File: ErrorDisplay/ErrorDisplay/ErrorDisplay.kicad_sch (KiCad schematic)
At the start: 0 parts

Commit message: Close Placement of Motors. Need Mechanical Fit check first
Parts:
- added H1, H2, H3, H4: MountingHole, MountingHole:MountingHole_4.3mm_M4, symbol Mechanical:MountingHole
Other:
- added sheet Motors (Motors.kicad_sch)
- note added: "Mounting Bracket to the faceplate"

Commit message: WIP - Test build for the Stepper Driver
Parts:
- added J4: Conn_01x04_Pin, Library:CONN_70551-xxxx_04_MOL, symbol Connector:Conn_01x04_Pin
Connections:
- new net CANH: J4.2 (Pin_2)
- new net CANL: J4.3 (Pin_3)
- new net CAN_VCC: J4.1 (Pin_1)
- new net GND: J4.4 (Pin_4)
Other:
- added sheet CANBus (CANBus.kicad_sch)
- added sheet MCU (MCU.kicad_sch)
- added sheet Power (Power.kicad_sch)

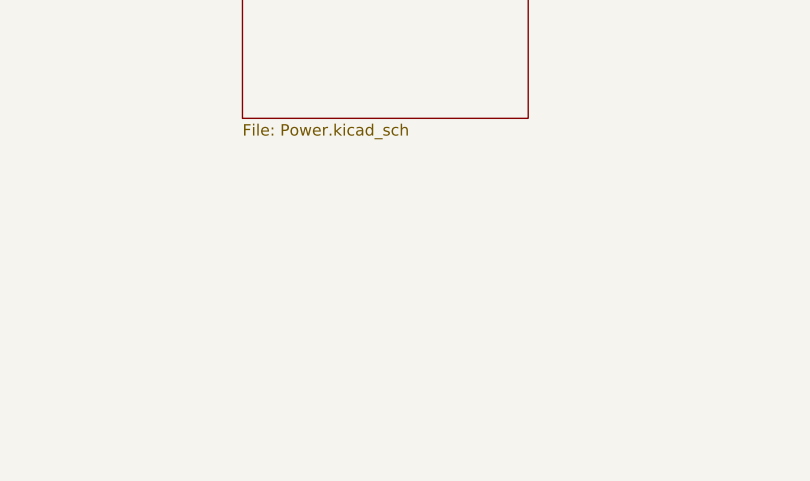
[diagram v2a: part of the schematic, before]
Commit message: LEDs outlined. Colors Chosen.
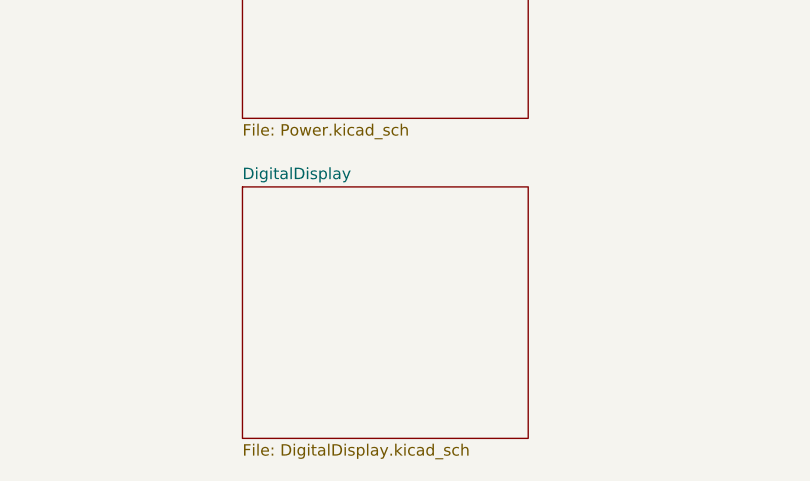
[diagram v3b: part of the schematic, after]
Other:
- added sheet DigitalDisplay (DigitalDisplay.kicad_sch)
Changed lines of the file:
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@@
+		)
+	)
+	(sheet
+		(at 68.58 162.56)
+		(size 31.75 27.94)
+		(fields_autoplaced yes)
+		(stroke
+			(width 0.1524)
+			(type solid)
+		)
+		(fill
+			(color 0 0 0 0.0000)
+		)
+		(property "Sheetname" "DigitalDisplay"
+			(at 68.58 161.8484 0)
+			(effects
+				(font
+					(size 1.27 1.27)
+				)
+				(justify left bottom)
+			)
+		)
+		(property "Sheetfile" "DigitalDisplay.kicad_sch"
+			(at 68.58 191.0846 0)
+			(effects
+				(font
+					(size 1.27 1.27)
+				)
+				(justify left top)
+			)
+		)
+		(instances
+			(project "ErrorDisplay"
+				(path "/96a9355b-dc07-421e-8192-6c91221ac38a"
+					(page "6")
+				)
+			)
 		)
 	)

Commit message: WIP checkin
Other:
- sheet DigitalDisplay ports: added SCL, SDA; removed none
- sheet MCU ports: added SCL, SDA; removed none
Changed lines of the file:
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@@
+		)
+	)
+	(label "SDA"
+		(at 100.33 166.37 0)
+		(fields_autoplaced yes)
+		(effects
+			(font
+				(size 1.27 1.27)
+			)
+			(justify left bottom)
 		)
 	)
@@
 			)
 			(justify left bottom)
+		)
+	)
+	(label "SCL"
+		(at 134.62 151.13 180)
+		(fields_autoplaced yes)
+		(effects
+			(font
+				(size 1.27 1.27)
+			)
+			(justify right bottom)
+		)
+	)
+	(label "SCL"
+		(at 100.33 163.83 0)
+		(fields_autoplaced yes)
+		(effects
+			(font
+				(size 1.27 1.27)
+			)
+			(justify left bottom)
+		)
+	)
+	(label "SDA"
+		(at 134.62 153.67 180)
+		(fields_autoplaced yes)
+		(effects
+			(font
+				(size 1.27 1.27)
+			)
+			(justify right bottom)
 		)
 	)
@@
 		)
 		(property "Sheetfile" "MCU.kicad_sch"
-			(at 132.334 154.94 90)
+			(at 132.334 142.24 90)
 			(effects
 				(font
@@
 				)
 				(justify right)
+			)
+		)
+		(pin "SDA" input
+			(at 134.62 153.67 180)
+			(effects
+				(font
+					(size 1.27 1.27)
+				)
+				(justify left)
+			)
+		)
+		(pin "SCL" input
+			(at 134.62 151.13 180)
+			(effects
+				(font
+					(size 1.27 1.27)
+				)
+				(justify left)
 			)
 		)
@@
 			)
 		)
+		(pin "SCL" input
+			(at 100.33 163.83 0)
+			(effects
+				(font
+					(size 1.27 1.27)
+				)
+				(justify right)
+			)
+		)
+		(pin "SDA" input
+			(at 100.33 166.37 0)
+			(effects
+				(font
+					(size 1.27 1.27)
+				)
+				(justify right)
+			)
+		)

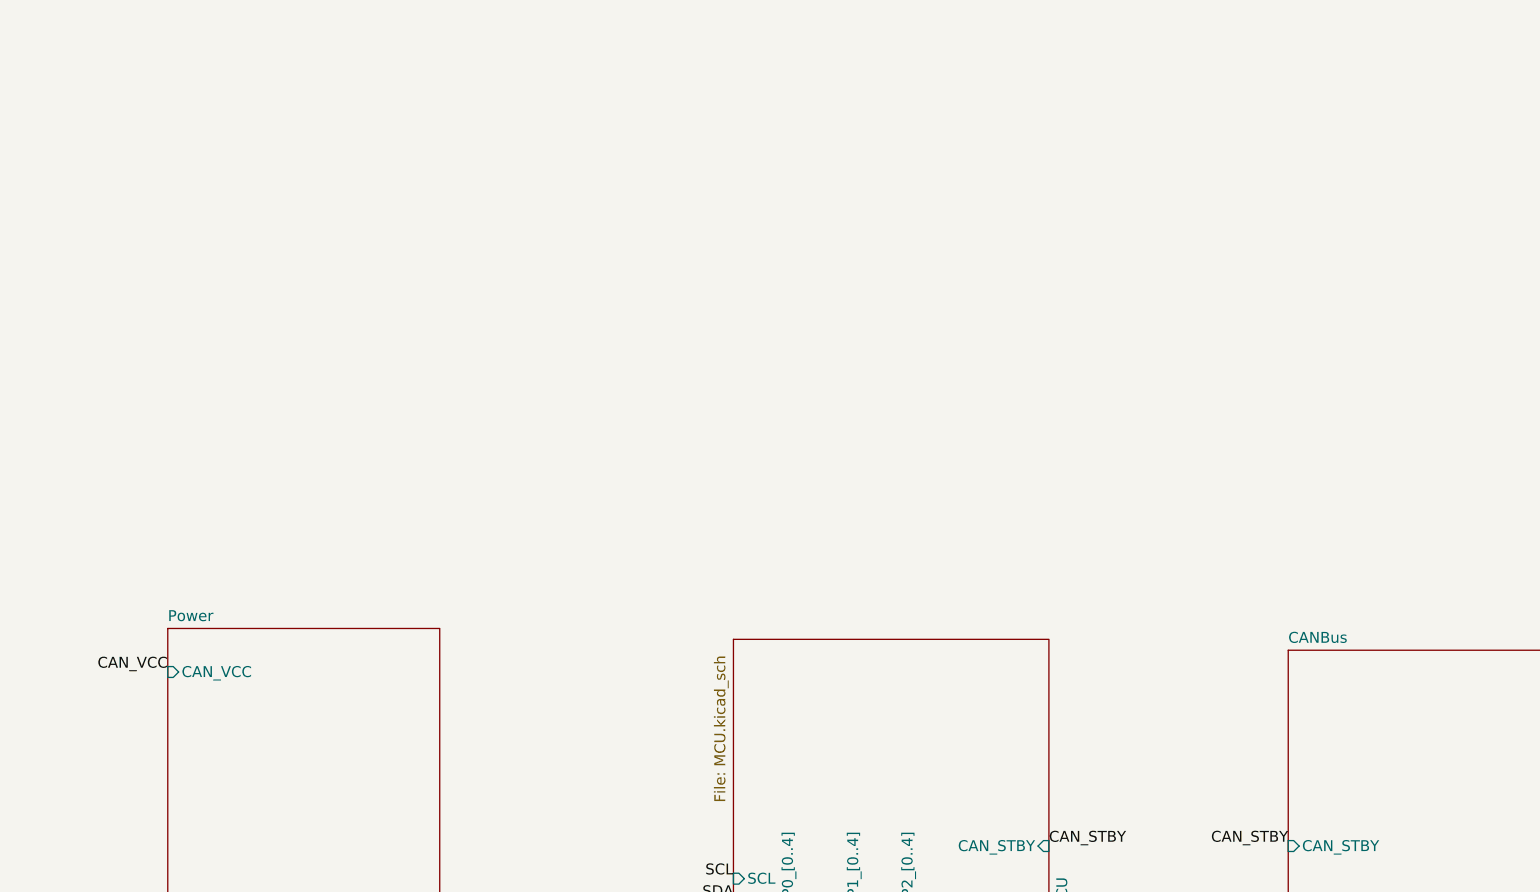
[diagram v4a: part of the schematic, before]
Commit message: Added Buzzer, Fet Footprint, and pulled backlighting
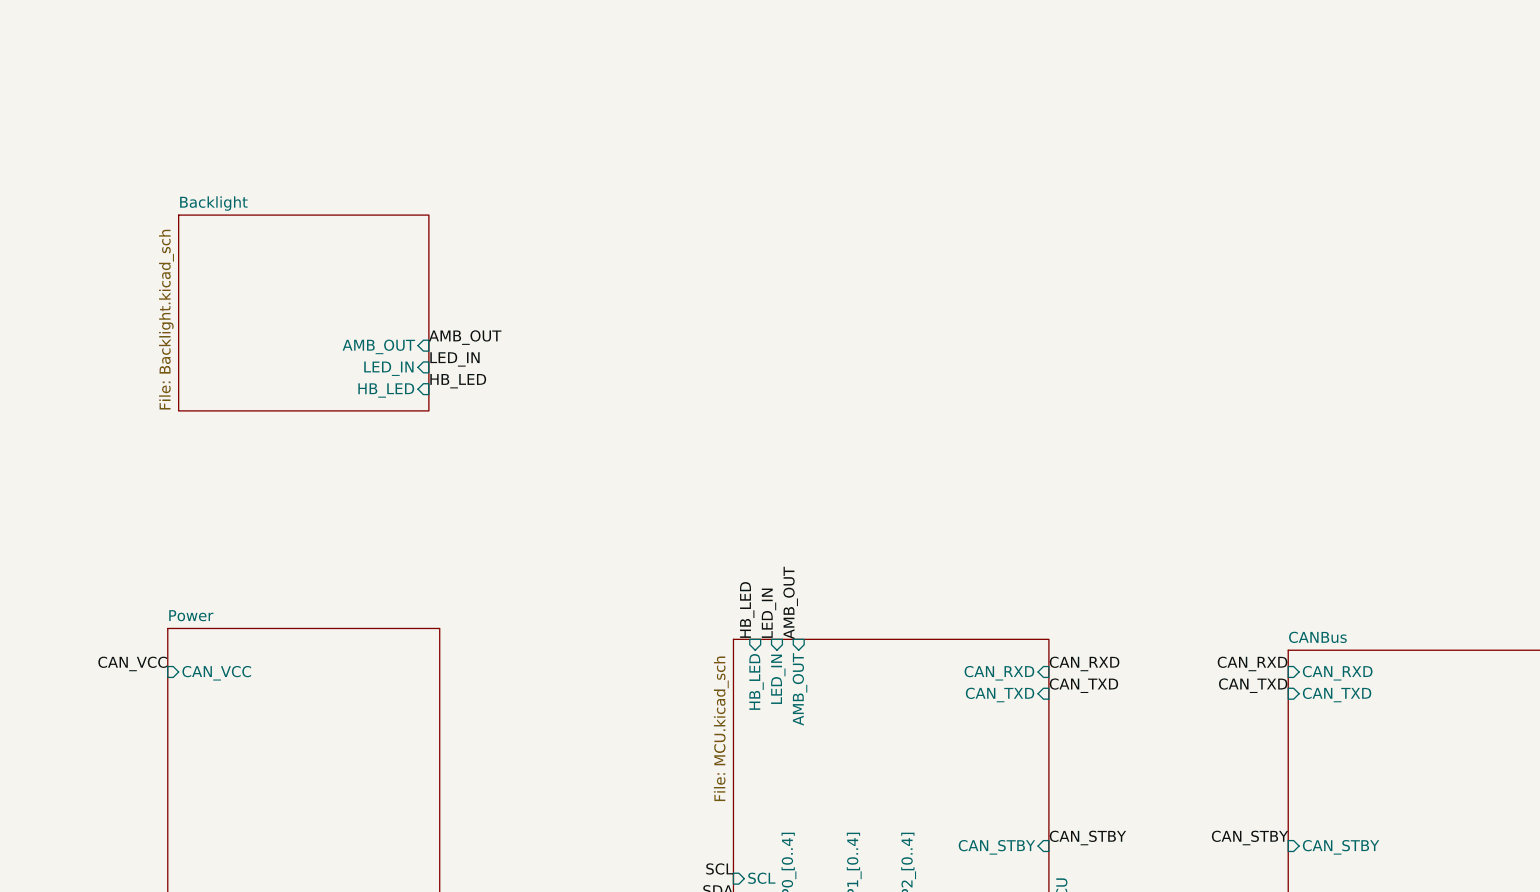
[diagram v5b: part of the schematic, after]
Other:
- added sheet Backlight (Backlight.kicad_sch)
- sheet CANBus ports: added CAN_RXD, CAN_TXD; removed none
- sheet MCU ports: added AMB_OUT, CAN_RXD, CAN_TXD, HB_LED, LED_IN; removed none
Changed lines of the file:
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@@
 	(label "CAN_VCC"
 		(at 271.78 19.05 180)
-		(fields_autoplaced yes)
 		(effects
 			(font
@@
 	(label "CANH"
 		(at 238.76 124.46 90)
-		(fields_autoplaced yes)
 		(effects
 			(font
@@
 	(label "SDA"
 		(at 100.33 166.37 0)
-		(fields_autoplaced yes)
 		(effects
 			(font
@@
 	(label "CAN_STBY"
 		(at 171.45 147.32 0)
-		(fields_autoplaced yes)
+		(effects
+			(font
+				(size 1.27 1.27)
+			)
+			(justify left bottom)
+		)
+	)
+	(label "AMB_OUT"
+		(at 142.24 123.19 90)
+		(effects
+			(font
+				(size 1.27 1.27)
+			)
+			(justify left bottom)
+		)
+	)
+	(label "CAN_RXD"
+		(at 199.39 127 180)
+		(effects
+			(font
+				(size 1.27 1.27)
+			)
+			(justify right bottom)
+		)
+	)
+	(label "HB_LED"
+		(at 99.06 93.98 0)
 		(effects
 			(font
@@
 	(label "CANL"
 		(at 271.78 24.13 180)
-		(fields_autoplaced yes)
 		(effects
 			(font
@@
 			)
 			(justify right bottom)
+		)
+	)
+	(label "LED_IN"
+		(at 139.7 123.19 90)
+		(effects
+			(font
+				(size 1.27 1.27)
+			)
+			(justify left bottom)
 		)
 	)
 	(label "CAN_STBY"
 		(at 199.39 147.32 180)
-		(fields_autoplaced yes)
 		(effects
 			(font
@@
 			)
 			(justify right bottom)
+		)
+	)
+	(label "CAN_TXD"
+		(at 171.45 129.54 0)
+		(effects
+			(font
+				(size 1.27 1.27)
+			)
+			(justify left bottom)
 		)
 	)
 	(label "GND"
 		(at 260.35 31.75 90)
-		(fields_autoplaced yes)
+		(effects
+			(font
+				(size 1.27 1.27)
+			)
+			(justify left bottom)
+		)
+	)
+	(label "LED_IN"
+		(at 99.06 91.44 0)
 		(effects
 			(font
@@
 	(label "SCL"
 		(at 134.62 151.13 180)
-		(fields_autoplaced yes)
 		(effects
 			(font
@@
 	(label "SCL"
 		(at 100.33 163.83 0)
-		(fields_autoplaced yes)
 		(effects
 			(font
@@
 	(label "SDA"
 		(at 134.62 153.67 180)
-		(fields_autoplaced yes)
 		(effects
 			(font
@@
 			)
 			(justify right bottom)
+		)
+	)
+	(label "AMB_OUT"
+		(at 99.06 88.9 0)
+		(effects
+			(font
+				(size 1.27 1.27)
+			)
+			(justify left bottom)
 		)
 	)
 	(label "CANL"
 		(at 241.3 124.46 90)
-		(fields_autoplaced yes)
 		(effects
 			(font
@@
 	(label "GND"
 		(at 271.78 26.67 180)
-		(fields_autoplaced yes)
 		(effects
 			(font
@@
 	(label "CAN_VCC"
 		(at 68.58 127 180)
-		(fields_autoplaced yes)
 		(effects
 			(font
@@
 			)
 			(justify right bottom)
+		)
+	)
+	(label "CAN_TXD"
+		(at 199.39 129.54 180)
+		(effects
+			(font
+				(size 1.27 1.27)
+			)
+			(justify right bottom)
+		)
+	)
+	(label "CAN_RXD"
+		(at 171.45 127 0)
+		(effects
+			(font
+				(size 1.27 1.27)
+			)
+			(justify left bottom)
+		)
+	)
+	(label "HB_LED"
+		(at 137.16 123.19 90)
+		(effects
+			(font
+				(size 1.27 1.27)
+			)
+			(justify left bottom)
 		)
 	)
 	(label "CANH"
 		(at 271.78 21.59 180)
-		(fields_autoplaced yes)
 		(effects
 			(font
@@
 	)
 	(sheet
+		(at 69.85 73.66)
+		(size 29.21 22.86)
+		(stroke
+			(width 0.1524)
+			(type solid)
+		)
+		(fill
+			(color 0 0 0 0.0000)
+		)
+		(property "Sheetname" "Backlight"
+			(at 69.85 72.9484 0)
+			(effects
+				(font
+					(size 1.27 1.27)
+				)
+				(justify left bottom)
+			)
+		)
+		(property "Sheetfile" "Backlight.kicad_sch"
+			(at 67.564 96.52 90)
+			(effects
+				(font
+					(size 1.27 1.27)
+				)
+				(justify left top)
+			)
+		)
+		(pin "LED_IN" input
+			(at 99.06 91.44 0)
+			(effects
+				(font
+					(size 1.27 1.27)
+				)
+				(justify right)
+			)
+		)
+		(pin "HB_LED" input
+			(at 99.06 93.98 0)
+			(effects
+				(font
+					(size 1.27 1.27)
+				)
+				(justify right)
+			)
+		)
+		(pin "AMB_OUT" input
+			(at 99.06 88.9 0)
+			(effects
+				(font
+					(size 1.27 1.27)
+				)
+				(justify right)
+			)
+		)
+		(instances
+			(project "ErrorDisplay"
+				(path "/96a9355b-dc07-421e-8192-6c91221ac38a"
+					(page "7")
+				)
+			)
+		)
+	)
+	(sheet
 		(at 134.62 123.19)
 		(size 36.83 31.75)
@@
 				)
 				(justify left)
+			)
+		)
+		(pin "HB_LED" input
+			(at 137.16 123.19 90)
+			(effects
+				(font
+					(size 1.27 1.27)
+				)
+				(justify right)
+			)
+		)
+		(pin "LED_IN" input
+			(at 139.7 123.19 90)
+			(effects
+				(font
+					(size 1.27 1.27)
+				)
+				(justify right)
+			)
+		)
+		(pin "AMB_OUT" input
+			(at 142.24 123.19 90)
+			(effects
+				(font
+					(size 1.27 1.27)
+				)
+				(justify right)
+			)
+		)
+		(pin "CAN_RXD" input
+			(at 171.45 127 0)
+			(effects
+				(font
+					(size 1.27 1.27)
+				)
+				(justify right)
+			)
+		)
+		(pin "CAN_TXD" input
+			(at 171.45 129.54 0)
+			(effects
+				(font
+					(size 1.27 1.27)
+				)
+				(justify right)
 			)
 		)
@@
 			)
 		)
+		(pin "CAN_RXD" input
+			(at 199.39 127 180)
+			(effects
+				(font
+					(size 1.27 1.27)
+				)
+				(justify left)
+			)
+		)
+		(pin "CAN_TXD" input
+			(at 199.39 129.54 180)
+			(effects
+				(font
+					(size 1.27 1.27)
+				)
+				(justify left)
+			)
+		)
